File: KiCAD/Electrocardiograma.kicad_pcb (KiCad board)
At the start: 2 copper layers, 56 parts, among them J3 AudioJack4, SW1 SW_DPST_x2, U1 INA823DT, U2 ESP32-C3-WROOM-02, U3 AMS1117-3.3, U3 TLV1117-33, U4 TLV4888, U5 TLV4888, U6 TLV1117-ADJ

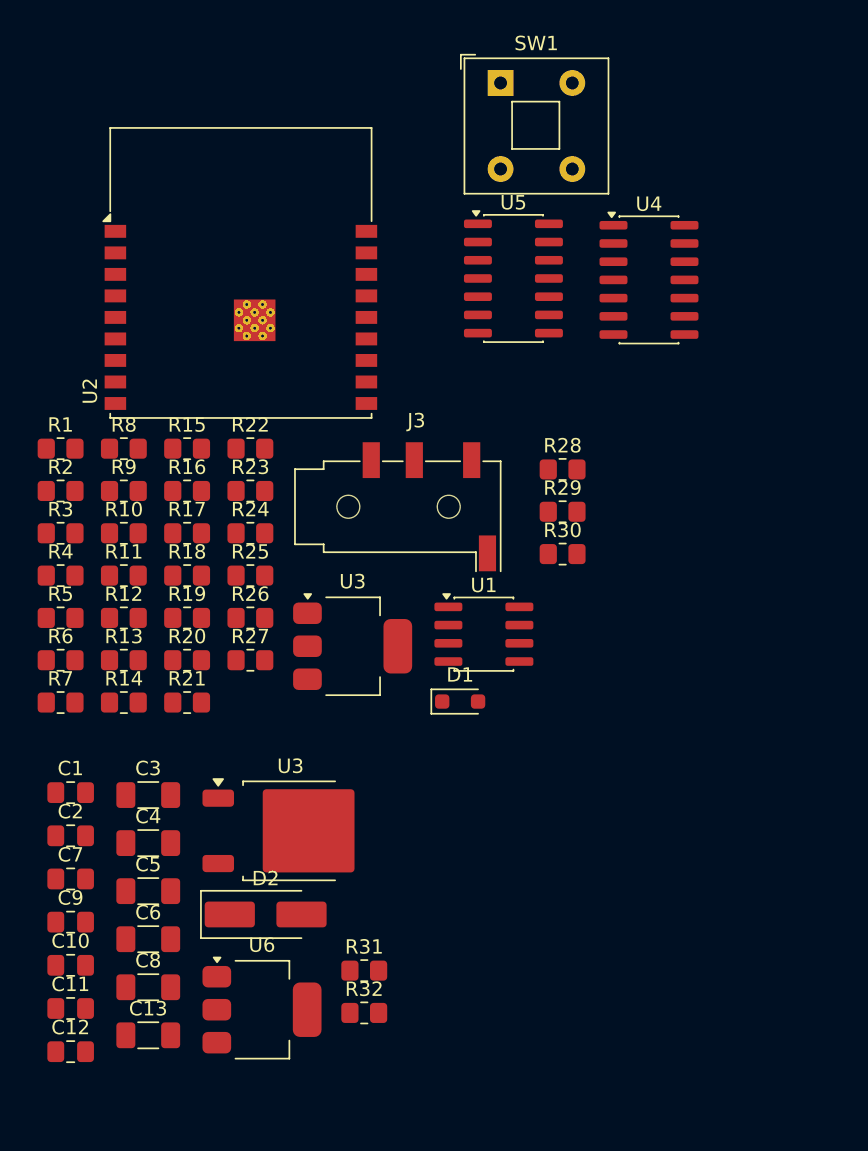
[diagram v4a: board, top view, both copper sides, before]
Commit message: Corte de placa y plano de tierra en botton y top layer
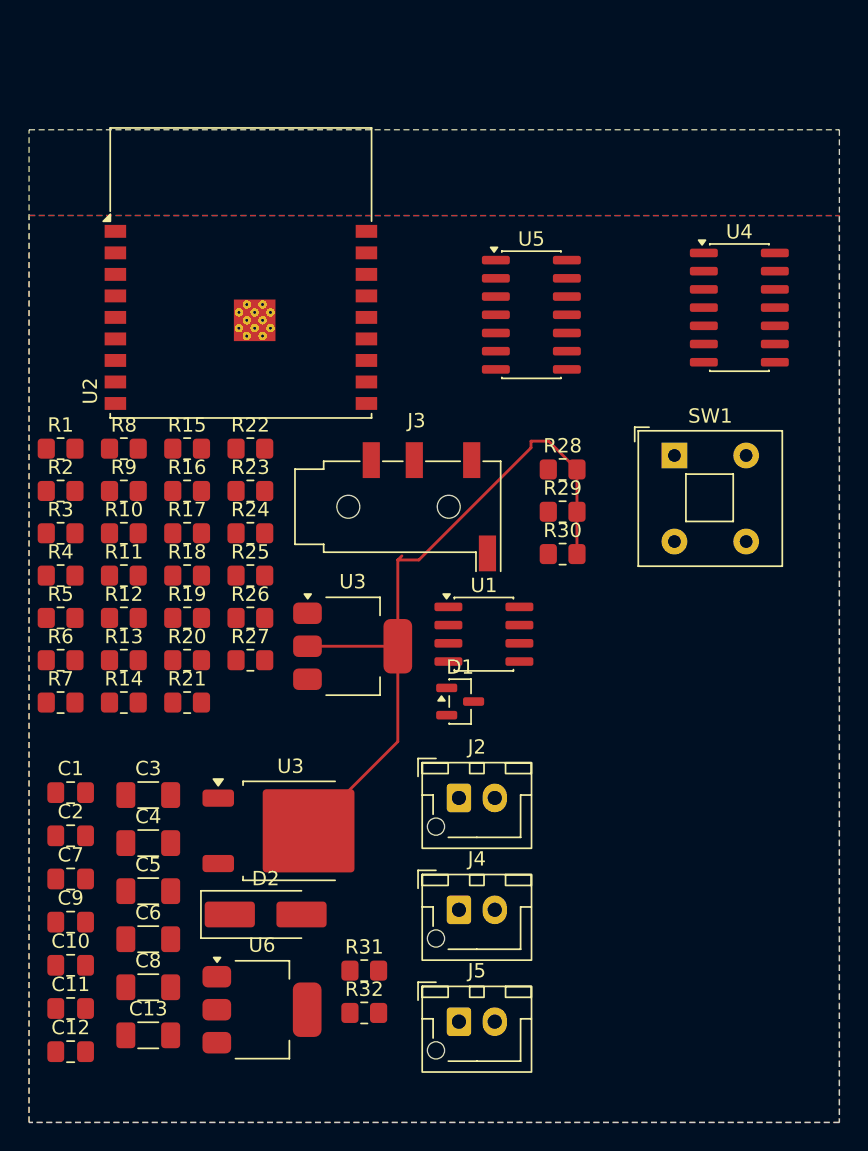
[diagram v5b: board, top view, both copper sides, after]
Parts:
- added J2: Conn_01x02_Pin, Connector_JST:JST_XH_B2B-XH-AM_1x02_P2.50mm_Vertical, F.Cu at (55.5, 73.4)
- added J4: Conn_01x02_Pin, Connector_JST:JST_XH_B2B-XH-AM_1x02_P2.50mm_Vertical, F.Cu at (55.5, 81.2)
- added J5: Conn_01x02_Pin, Connector_JST:JST_XH_B2B-XH-AM_1x02_P2.50mm_Vertical, F.Cu at (55.5, 89.0)
- D1: footprint Diode_SMD:D_SOD-323_HandSoldering -> Package_TO_SOT_SMD:SOT-23
- moved SW1 28.7 mm to (70.5, 49.5)
- moved U4 6.59 mm to (75.0, 39.2)
- moved U5 2.82 mm to (60.5, 39.7)
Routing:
- net +3.3V: track 0.00 -> 51.1 mm
- added copper zone on B.Cu, net -BATT_REG
- added copper zone on F.Cu, net -BATT_REG
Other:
- board outline added: 56.5 x 69.2 mm

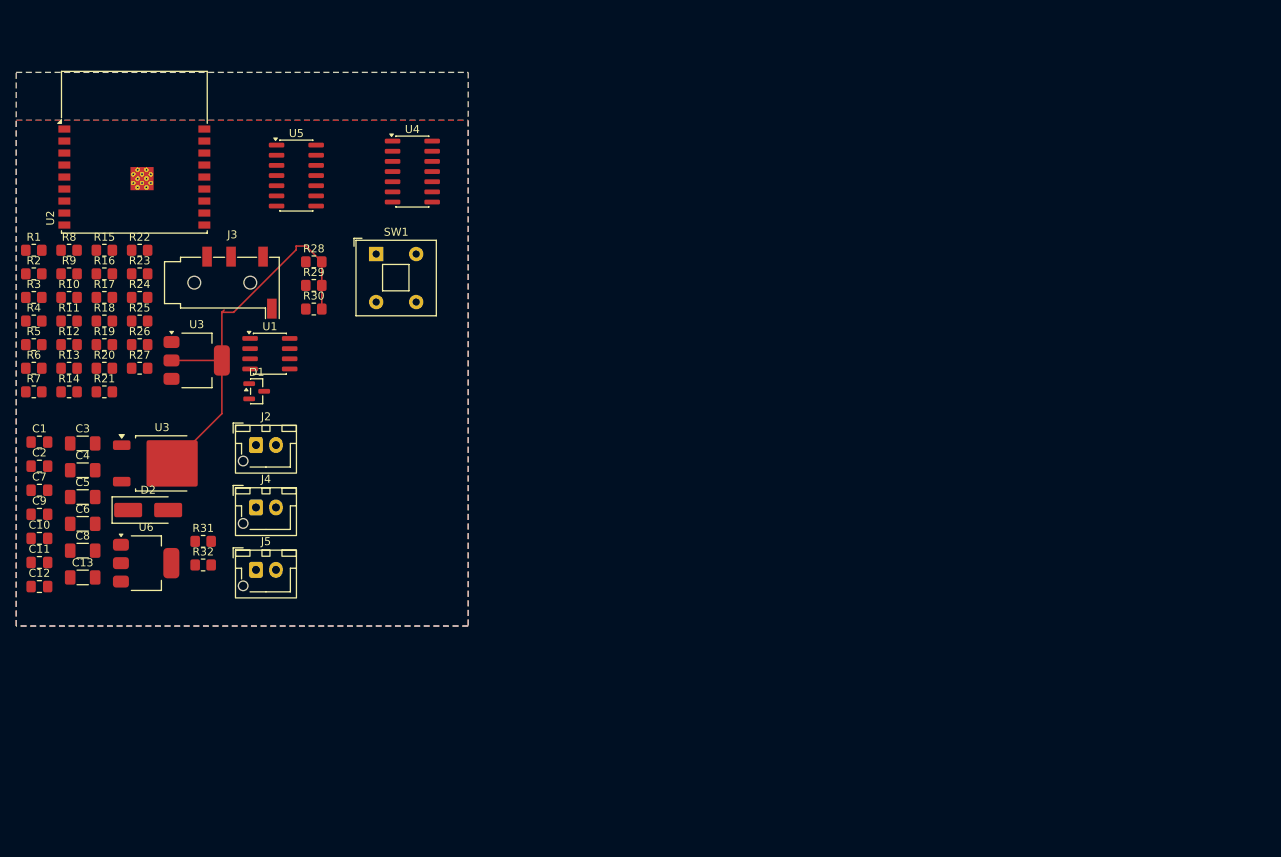
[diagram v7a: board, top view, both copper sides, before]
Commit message: Added an opamp to condition the sensed signal for the esp32, also adjust PCB component positions & footprints
Add a differential opamp to change the singal's mounted voltaje, from 3.05V, to 1.65V, so it's in operation range for the ADC of the ESP32 . Move multiple PCB footprints and update footprint metadata.
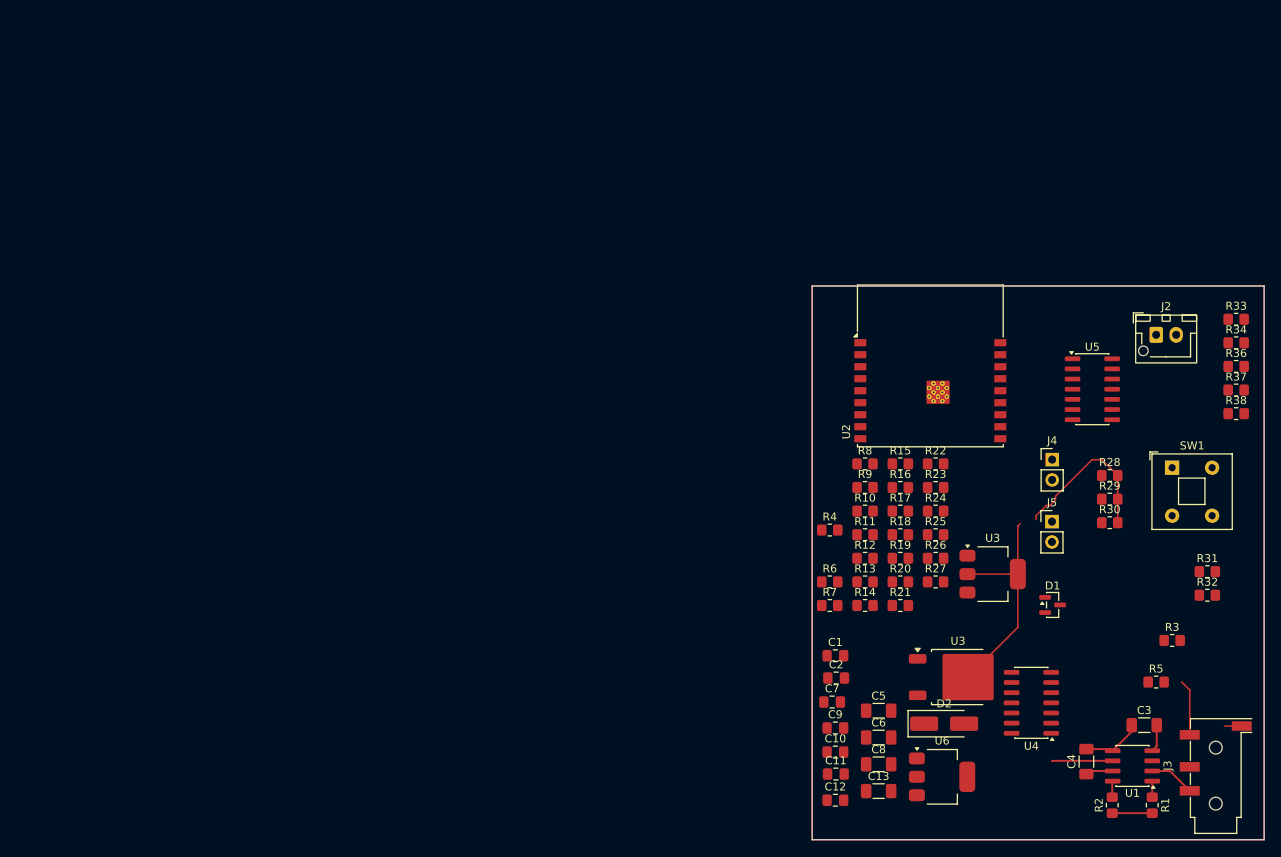
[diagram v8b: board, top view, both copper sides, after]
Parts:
- added R33: 100K, Resistor_SMD:R_0805_2012Metric_Pad1.20x1.40mm_HandSolder, F.Cu at (178.0, 57.6)
- added R34: 100K, Resistor_SMD:R_0805_2012Metric_Pad1.20x1.40mm_HandSolder, F.Cu at (178.0, 60.6)
- added R36: 100K, Resistor_SMD:R_0805_2012Metric_Pad1.20x1.40mm_HandSolder, F.Cu at (178.0, 63.5)
- added R37: 150K, Resistor_SMD:R_0805_2012Metric_Pad1.20x1.40mm_HandSolder, F.Cu at (178.0, 66.5)
- added R38: 100K, Resistor_SMD:R_0805_2012Metric_Pad1.20x1.40mm_HandSolder, F.Cu at (178.0, 69.5)
- J4, J5: footprint Connector_JST:JST_XH_B2B-XH-AM_1x02_P2.50mm_Vertical -> Connector_PinHeader_2.54mm:PinHeader_1x02_P2.54mm_Vertical
- moved R1 156.1 mm to (167.5, 118.4), turned to -90 degrees
- moved R2 150.3 mm to (162.5, 118.4), turned to 90 degrees
- moved R3 148.6 mm to (170.0, 97.8)
- moved R5 146.5 mm to (168.0, 103.0)
- moved C3 137.3 mm to (166.5, 108.4)
- moved J3 137.0 mm to (175.4, 113.5), turned to 90 degrees
- moved C4 130.6 mm to (159.3, 112.9), turned to 90 degrees
- moved R31 125.6 mm to (174.4, 89.2)
- moved R32 125.6 mm to (174.4, 92.2)
- moved U1 119.5 mm to (165.0, 113.5), turned to 180 degrees
- moved J2 113.4 mm to (168.0, 59.6)
- moved C2 103.1 mm to (128.0, 102.5)
- moved C13 103.0 mm to (133.3, 116.6)
- moved C5 103.0 mm to (133.3, 106.6)
- moved C6 103.0 mm to (133.3, 109.9)
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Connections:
- D1 pad 1: +BATT_REG -> +BATT
- D2 pad 2: Net-(D2-A) -> +BATT
- SW1 pad 2: Net-(D2-A) -> +BATT
- U1 pad 7: +5.0V -> +6.1V
- U4 pad 12: (no net) -> Net-(U4D-+)
- U4 pad 13: (no net) -> Net-(U4D--)
- U4 pad 14: (no net) -> /To_ESP32
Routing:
- net /<NO NET>: track 0.00 -> 7.57 mm
- net GND: track 0.00 -> 7.54 mm
- net Net-(J3-PadT): track 0.00 -> 7.01 mm
- net Net-(U1--): track 0.00 -> 5.72 mm
- net Net-(U4A-+): track 0.00 -> 5.00 mm
- net +6.1V: track 0.00 -> 3.52 mm
- net -BATT_REG: track 0.00 -> 3.42 mm
- net Net-(U1-+): track 0.00 -> 2.39 mm
- net +3.3V: track 51.1 -> 48.8 mm
- net Net-(R2-Pad2): track 0.00 -> 2.02 mm
- net Net-(R1-Pad1): track 0.00 -> 2.00 mm
- removed copper zone on B.Cu, net -BATT_REG
- removed copper zone on F.Cu, net -BATT_REG
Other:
- board text added: "Que tan criminal es hacer esto?"
- board text added: "Recuerdo que me dijiste que igual si se hacía"
